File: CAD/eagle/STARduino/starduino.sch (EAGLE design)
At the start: 129 parts, among them J1 J30J-9, J2 MICRO_SD, J3 J30J-15, J4 J30J-31, J5 RPI-ZERO, J6 RPI-CSI, Q1 FDG8842CZ, Q2 FDG8842CZ, Q3 DMMT5401, Q4 DMG2305UX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

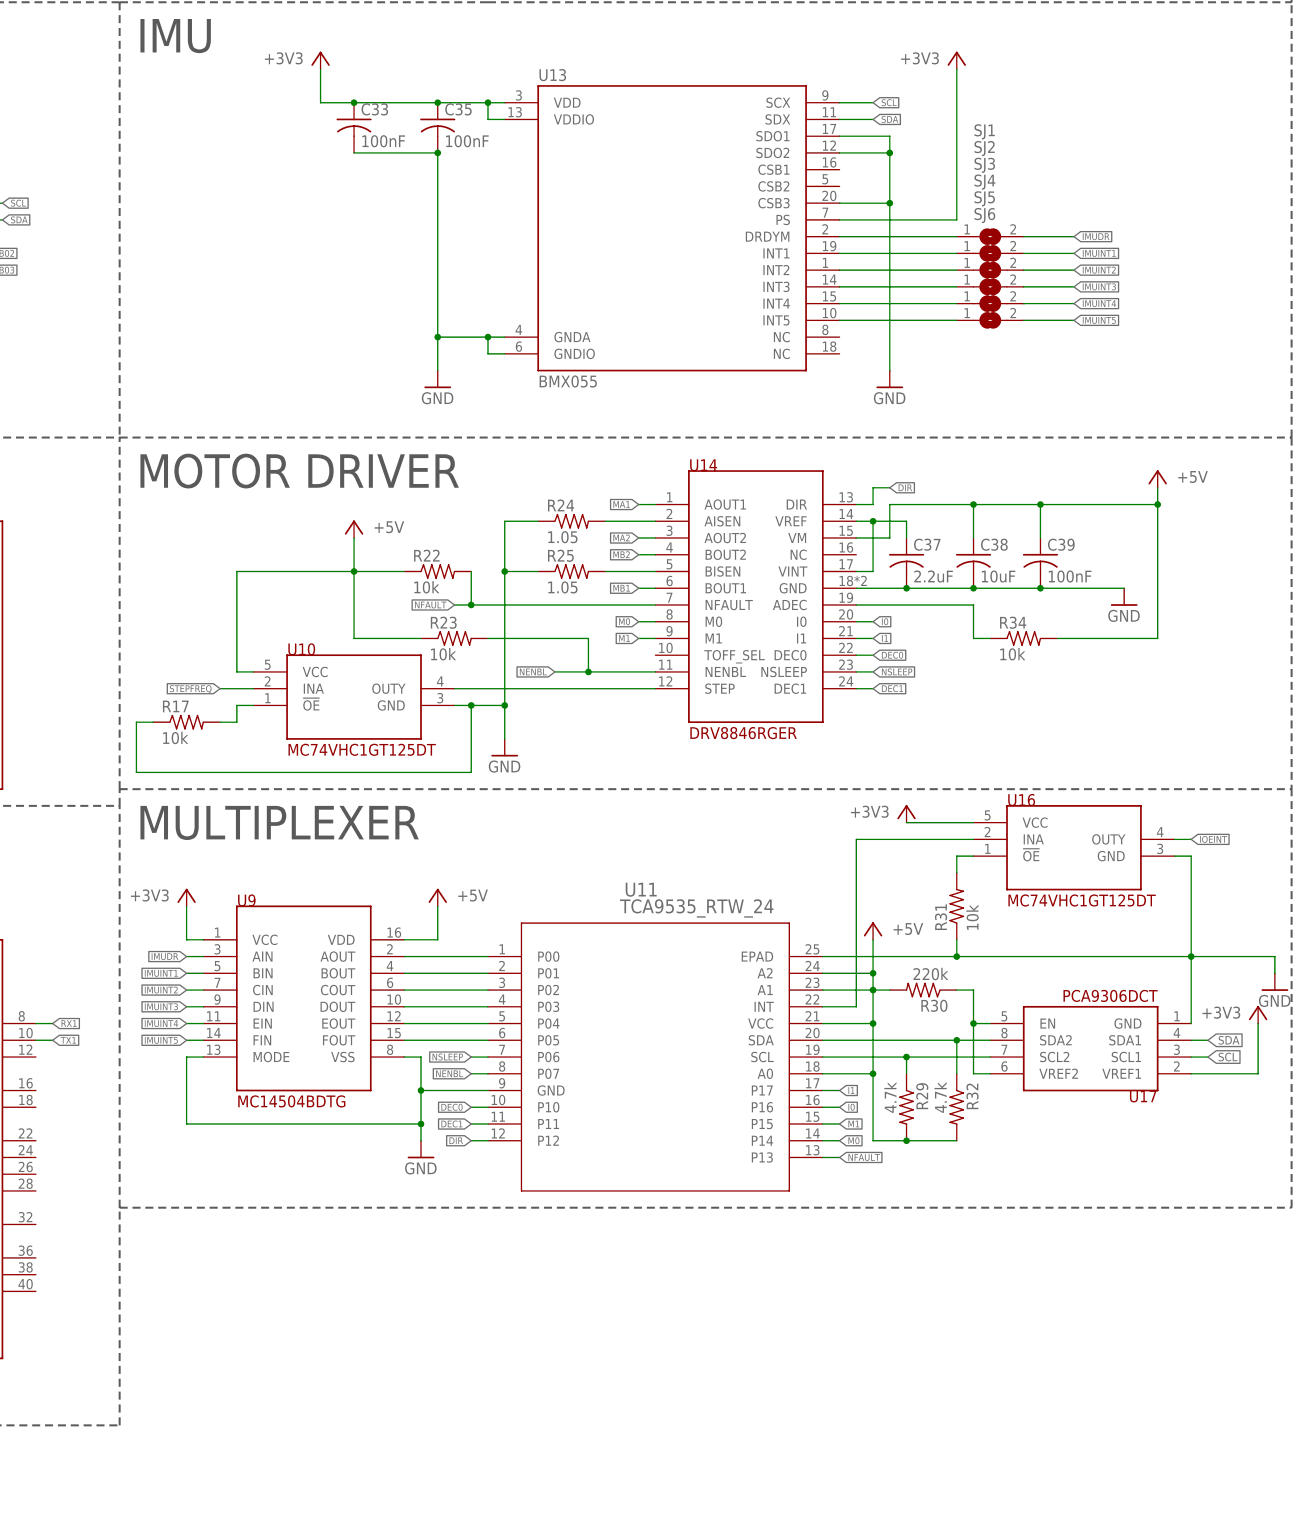
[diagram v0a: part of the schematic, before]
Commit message: Cleaned up some symbols
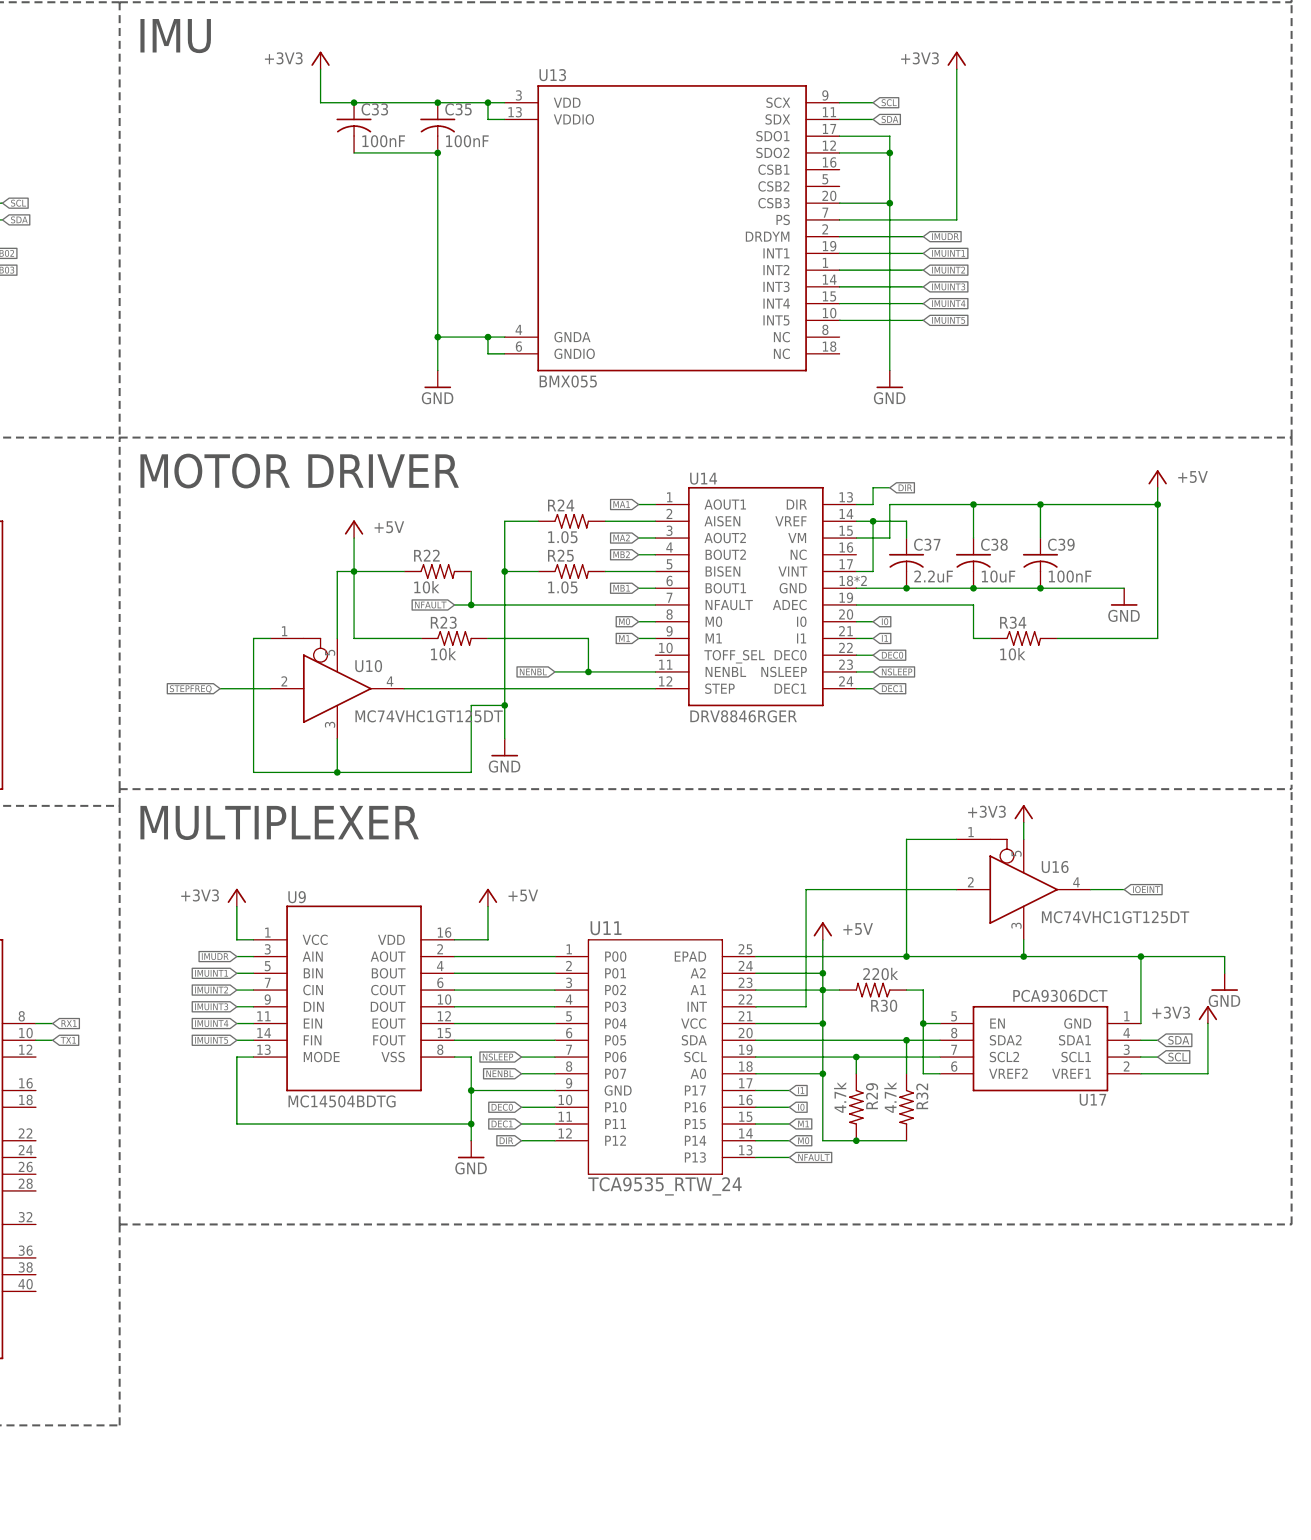
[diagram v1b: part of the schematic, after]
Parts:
- removed R17, R31: 10k, rcl:R-US_R0603
- removed SJ1, SJ2, SJ3, SJ4, SJ5, SJ6: (no value), jumper:SJ
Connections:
- removed net N$10: SJ2.1, U13.INT1
- removed net N$11: SJ3.1, U13.INT2
- removed net N$12: SJ4.1, U13.INT3
- removed net N$13: SJ5.1, U13.INT4
- removed net N$14: SJ6.1, U13.INT5
- removed net N$24: R17.2, U10.!OE!
- removed net N$27: R31.2, U16.!OE!
- removed net N$9: SJ1.1, U13.DRDYM
- net GND: now also U10.!OE!, U16.!OE!; no longer R17.1, R31.1
- net IMUDR: now also U13.DRDYM; no longer SJ1.2
- net IMUINT1: now also U13.INT1; no longer SJ2.2
- net IMUINT2: now also U13.INT2; no longer SJ3.2
- net IMUINT3: now also U13.INT3; no longer SJ4.2
- net IMUINT4: now also U13.INT4; no longer SJ5.2
- net IMUINT5: now also U13.INT5; no longer SJ6.2
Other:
- moved on the sheet: R29, R30, R32, U17, U9

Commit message: Schematic updates
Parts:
- removed S1: PTS525-SM15, AR_switches:PTS525-SM15
- added JP2: (no value), CM_passives:JUMPER-2PTH
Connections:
- net CAM1_DN1 renamed CAM1_D1_N
- net CAM1_DP1 renamed CAM1_D1_P
- net N$44 renamed COMP_5
- net N$45 renamed FB_5
- removed net CAM1_CN: J4.24, J6.CAM1_CN
- removed net CAM1_CP: J4.25, J6.CAM1_CP
- removed net CAM1_DN0: J4.18, J6.CAM1_DN0
- removed net CAM1_DP0: J4.19, J6.CAM1_DP0
- removed net N$47: C12.1, R5.1, U3.IOUT
- new net CAM1_C_N: J4.25, J6.CAM1_CN
- new net CAM1_C_P: J4.24, J6.CAM1_CP
- new net CAM1_D0_N: J4.19, J6.CAM1_DN0
- new net CAM1_D0_P: J4.18, J6.CAM1_DP0
- net GND: now also J1.3, J1.4, JP2.1; no longer J1.2, S1.1, S1.2
- net I_SENSE: now also C12.1, R5.1, U3.IOUT
- net N$7: now also JP2.2; no longer S1.3, S1.4
- net PWM/SYNC: now also U6.PA14/XIN/EIC/SCOM2PAD2+/TC3
- net SYNC: now also J5.BCM26
- net VCC: now also J1.2
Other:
- moved on the sheet: B1, C1, C10, C11, C12, C13, C14, C15, C16, C17, C18, C19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

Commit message: Layout and schematic progress
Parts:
- added TP1, TP2: TESTPOINT, CM_passives:TESTPOINT
- J1: value J30J-9 -> J30J-9J30; device CM_J30J:J30J-9 -> CM_J30J:J30J-9J30
- J3: value J30J-15 -> J30J-15J30; device CM_J30J:J30J-15 -> CM_J30J:J30J-15J30
- J4: value J30J-31 -> J30J-31J30; device CM_J30J:J30J-31 -> CM_J30J:J30J-31J30
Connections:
- removed net C_GND: J4.17, J4.20, J4.23, J4.26, J6.GND1, J6.GND2, J6.GND3, J6.GND4
- removed net PI_D+: J3.7
- removed net PI_D1: J3.8
- new net PI_D_N: J3.8, TP2.P$1
- new net PI_D_P: J3.7, TP1.P$1
- new net USB_D_N: J3.4
- new net USB_D_P: J3.3
- net BIAS_GND: now also J4.3; no longer J4.4
- net BIAS_V: now also J4.4; no longer J4.3
- net CAM1_C_N: now also J4.24; no longer J4.25
- net CAM1_C_P: now also J4.25; no longer J4.24
- net CAM1_D0_N: now also J4.18; no longer J4.19
- net CAM1_D0_P: now also J4.19; no longer J4.18
- net GND: now also J4.17, J4.20, J4.23, J4.26, J6.GND1, J6.GND2, J6.GND3, J6.GND4
- net USB_D+: no longer J3.3
- net USB_D-: no longer J3.4

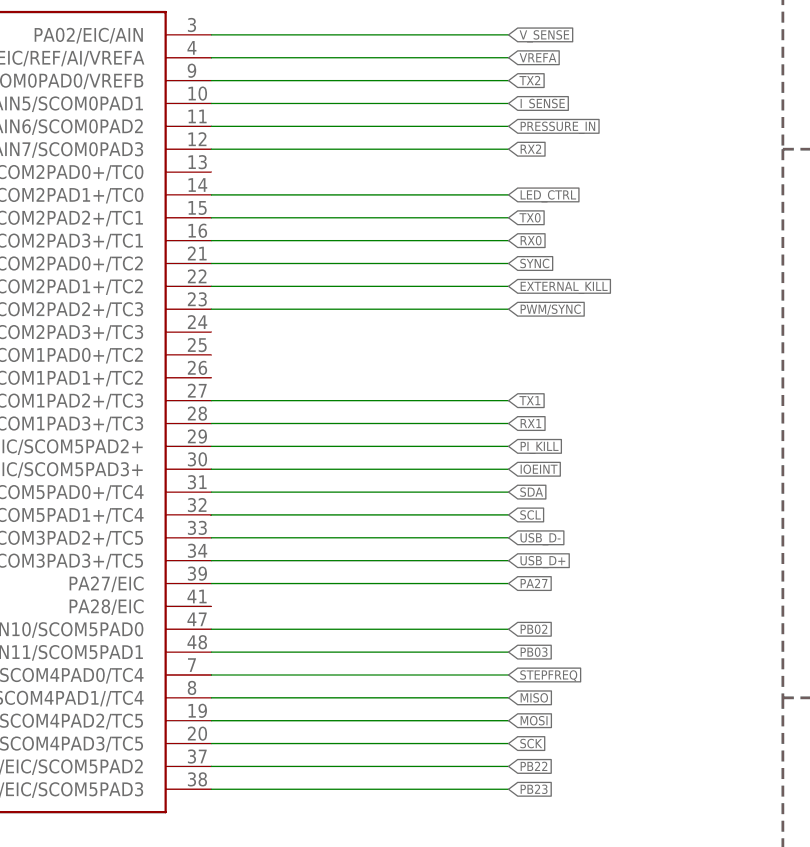
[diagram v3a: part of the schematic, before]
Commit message: Fixed STEPFREQ schematic bug.
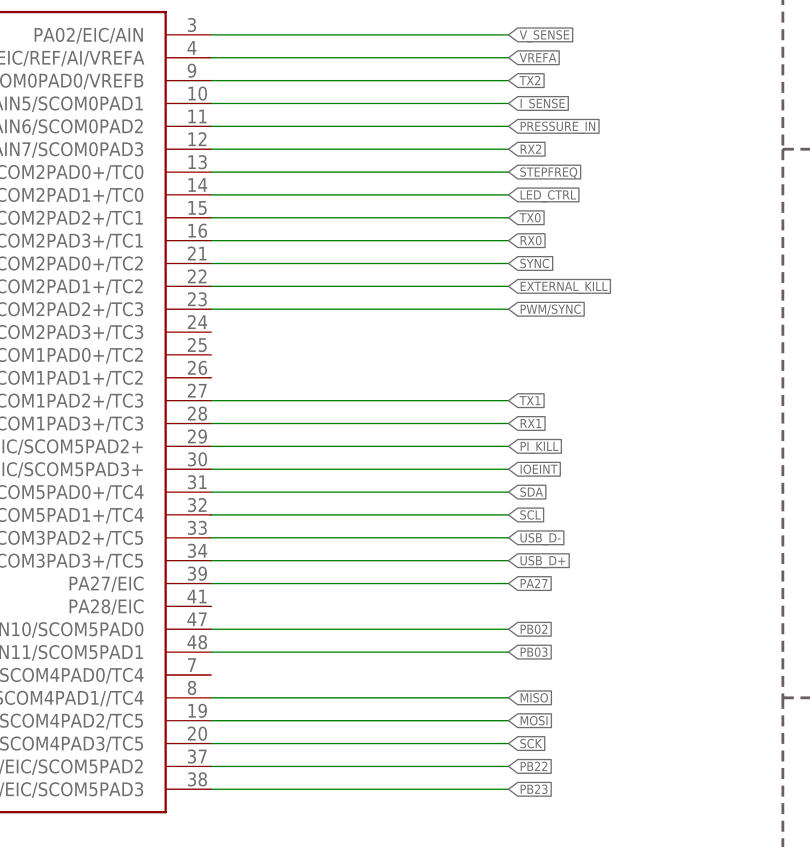
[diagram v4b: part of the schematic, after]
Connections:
- net STEPFREQ: now also U6.PA08/I2C/AIN16/SCOM2PAD0+/TC0; no longer U6.PB08/EIC/AIN2/SCOM4PAD0/TC4
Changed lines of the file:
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@@
 <?xml version="1.0" encoding="utf-8"?>
 <!DOCTYPE eagle SYSTEM "eagle.dtd">
-<eagle version="6.5.0">
+<eagle version="7.7.0">
 <drawing>
 <settings>
@@
 </segment>
 <segment>
-<pinref part="U6" gate="G$1" pin="PB08/EIC/AIN2/SCOM4PAD0/TC4"/>
-<wire x1="312.42" y1="327.66" x2="345.44" y2="327.66" width="0.1524" layer="91"/>
-<label x="345.44" y="327.66" size="1.016" layer="95" xref="yes"/>
-</segment>
-</net>
+<pinref part="U6" gate="G$1" pin="PA08/I2C/AIN16/SCOM2PAD0+/TC0"/>
+<wire x1="312.42" y1="383.54" x2="345.44" y2="383.54" width="0.1524" layer="91"/>
+<label x="345.44" y="383.54" size="1.016" layer="95" xref="yes"/>
+</segment>
+</net>

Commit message: Board routing
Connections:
- net DEC0: now also U11.P15; no longer U11.P10
- net DEC1: now also U11.P13; no longer U11.P11
- net I0: now also U11.P17; no longer U11.P16
- net I1: now also U11.P16; no longer U11.P17
- net M0: now also U11.P06; no longer U11.P14
- net M1: now also U11.P10; no longer U11.P15
- net NFAULT: now also U11.P11; no longer U11.P13
- net NSLEEP: now also U11.P14; no longer U11.P06
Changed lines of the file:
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@@
 <?xml version="1.0" encoding="utf-8"?>
 <!DOCTYPE eagle SYSTEM "eagle.dtd">
-<eagle version="7.7.0">
+<eagle version="6.5.0">
 <drawing>
 <settings>
@@
 </segment>
 <segment>
-<pinref part="U11" gate="A" pin="P13"/>
-<wire x1="472.44" y1="116.84" x2="477.52" y2="116.84" width="0.1524" layer="91"/>
-<label x="477.52" y="116.84" size="1.016" layer="95" xref="yes"/>
+<pinref part="U11" gate="A" pin="P11"/>
+<wire x1="441.96" y1="121.92" x2="436.88" y2="121.92" width="0.1524" layer="91"/>
+<label x="436.88" y="121.92" size="1.016" layer="95" rot="R180" xref="yes"/>
 </segment>
 </net>
@@
 </segment>
 <segment>
-<label x="436.88" y="132.08" size="1.016" layer="95" rot="R180" xref="yes"/>
-<pinref part="U11" gate="A" pin="P06"/>
-<wire x1="436.88" y1="132.08" x2="441.96" y2="132.08" width="0.1524" layer="91"/>
+<pinref part="U11" gate="A" pin="P14"/>
+<wire x1="472.44" y1="119.38" x2="477.52" y2="119.38" width="0.1524" layer="91"/>
+<label x="477.52" y="119.38" size="1.016" layer="95" xref="yes"/>
 </segment>
 </net>
@@
 </segment>
 <segment>
+<pinref part="U11" gate="A" pin="P17"/>
+<wire x1="472.44" y1="127" x2="477.52" y2="127" width="0.1524" layer="91"/>
+<label x="477.52" y="127" size="1.016" layer="95" xref="yes"/>
+</segment>
+</net>
+<net name="I1" class="0">
+<segment>
+<pinref part="U14" gate="G$1" pin="I1"/>
+<wire x1="487.68" y1="195.58" x2="490.22" y2="195.58" width="0.1524" layer="91"/>
+<label x="490.22" y="195.58" size="1.016" layer="95" xref="yes"/>
+</segment>
+<segment>
 <pinref part="U11" gate="A" pin="P16"/>
 <wire x1="472.44" y1="124.46" x2="477.52" y2="124.46" width="0.1524" layer="91"/>
@@
 </segment>
 </net>
-<net name="I1" class="0">
-<segment>
-<pinref part="U14" gate="G$1" pin="I1"/>
-<wire x1="487.68" y1="195.58" x2="490.22" y2="195.58" width="0.1524" layer="91"/>
-<label x="490.22" y="195.58" size="1.016" layer="95" xref="yes"/>
-</segment>
-<segment>
-<pinref part="U11" gate="A" pin="P17"/>
-<wire x1="472.44" y1="127" x2="477.52" y2="127" width="0.1524" layer="91"/>
-<label x="477.52" y="127" size="1.016" layer="95" xref="yes"/>
-</segment>
-</net>
 <net name="M0" class="0">
 <segment>
@@
 </segment>
 <segment>
-<pinref part="U11" gate="A" pin="P14"/>
-<wire x1="472.44" y1="119.38" x2="477.52" y2="119.38" width="0.1524" layer="91"/>
-<label x="477.52" y="119.38" size="1.016" layer="95" xref="yes"/>
+<label x="436.88" y="132.08" size="1.016" layer="95" rot="R180" xref="yes"/>
+<pinref part="U11" gate="A" pin="P06"/>
+<wire x1="436.88" y1="132.08" x2="441.96" y2="132.08" width="0.1524" layer="91"/>
 </segment>
 </net>
@@
 </segment>
 <segment>
-<pinref part="U11" gate="A" pin="P15"/>
-<wire x1="472.44" y1="121.92" x2="477.52" y2="121.92" width="0.1524" layer="91"/>
-<label x="477.52" y="121.92" size="1.016" layer="95" xref="yes"/>
+<pinref part="U11" gate="A" pin="P10"/>
+<wire x1="441.96" y1="124.46" x2="436.88" y2="124.46" width="0.1524" layer="91"/>
+<label x="436.88" y="124.46" size="1.016" layer="95" rot="R180" xref="yes"/>
 </segment>
 </net>
@@
 </segment>
 <segment>
-<pinref part="U11" gate="A" pin="P10"/>
-<wire x1="441.96" y1="124.46" x2="436.88" y2="124.46" width="0.1524" layer="91"/>
-<label x="436.88" y="124.46" size="1.016" layer="95" rot="R180" xref="yes"/>
+<pinref part="U11" gate="A" pin="P15"/>
+<wire x1="472.44" y1="121.92" x2="477.52" y2="121.92" width="0.1524" layer="91"/>
+<label x="477.52" y="121.92" size="1.016" layer="95" xref="yes"/>
 </segment>
 </net>
@@
 </segment>
 <segment>
-<pinref part="U11" gate="A" pin="P11"/>
-<wire x1="441.96" y1="121.92" x2="436.88" y2="121.92" width="0.1524" layer="91"/>
-<label x="436.88" y="121.92" size="1.016" layer="95" rot="R180" xref="yes"/>
-</segment>
-</net>
+<pinref part="U11" gate="A" pin="P13"/>
+<wire x1="472.44" y1="116.84" x2="477.52" y2="116.84" width="0.1524" layer="91"/>
+<label x="477.52" y="116.84" size="1.016" layer="95" xref="yes"/>
+</segment>
+</net>

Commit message: Fixed Arduino fuckery
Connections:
- net MISO: now also U6.PA12/I2C/EIC/SCOM2PAD0+/TC2; no longer U6.PB09/EIC/AIN3/SCOM4PAD1//TC4
- net SYNC: now also U6.PA15/XOUT/EIC/SCOM2PAD3+/TC3; no longer U6.PA12/I2C/EIC/SCOM2PAD0+/TC2
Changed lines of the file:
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@@
 <?xml version="1.0" encoding="utf-8"?>
 <!DOCTYPE eagle SYSTEM "eagle.dtd">
-<eagle version="6.5.0">
+<eagle version="7.7.0">
 <drawing>
 <settings>
@@
 </segment>
 <segment>
-<pinref part="U6" gate="G$1" pin="PB09/EIC/AIN3/SCOM4PAD1//TC4"/>
-<wire x1="312.42" y1="325.12" x2="345.44" y2="325.12" width="0.1524" layer="91"/>
-<label x="345.44" y="325.12" size="1.016" layer="95" xref="yes"/>
+<pinref part="U6" gate="G$1" pin="PA12/I2C/EIC/SCOM2PAD0+/TC2"/>
+<wire x1="312.42" y1="373.38" x2="345.44" y2="373.38" width="0.1524" layer="91"/>
+<label x="345.44" y="373.38" size="1.016" layer="95" xref="yes"/>
 </segment>
 </net>
@@
 <net name="SYNC" class="0">
 <segment>
-<pinref part="U6" gate="G$1" pin="PA12/I2C/EIC/SCOM2PAD0+/TC2"/>
-<wire x1="312.42" y1="373.38" x2="345.44" y2="373.38" width="0.1524" layer="91"/>
-<label x="345.44" y="373.38" size="1.016" layer="95" xref="yes"/>
-</segment>
-<segment>
 <pinref part="J5" gate="G$1" pin="BCM26"/>
 <wire x1="317.5" y1="96.52" x2="314.96" y2="96.52" width="0.1524" layer="91"/>
 <label x="314.96" y="96.52" size="1.016" layer="95" rot="R180" xref="yes"/>
 </segment>
-</net>
+<segment>
+<pinref part="U6" gate="G$1" pin="PA15/XOUT/EIC/SCOM2PAD3+/TC3"/>
+<wire x1="312.42" y1="365.76" x2="345.44" y2="365.76" width="0.1524" layer="91"/>
+<label x="345.44" y="365.76" size="1.016" layer="95" xref="yes"/>
+</segment>
+</net>
